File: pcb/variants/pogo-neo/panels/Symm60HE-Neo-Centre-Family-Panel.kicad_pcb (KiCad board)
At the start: 2 copper layers, 73.4 x 52.4 mm, 102 parts

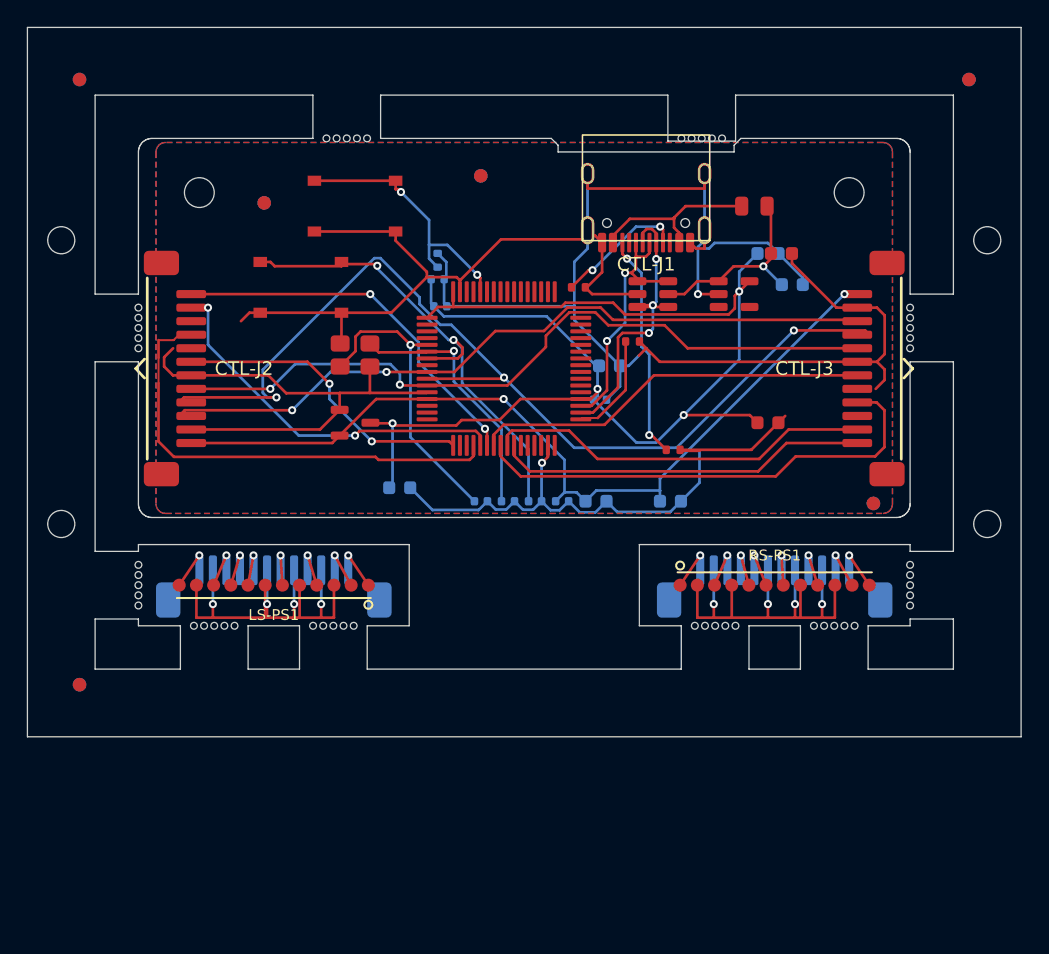
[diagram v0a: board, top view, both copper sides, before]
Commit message: Controller 57 x 27 mm straight rear edge; FPC jumpers into ZIF connectors; Neo Ergo mounting topology
Extend the former local J1 setback across the complete rear edge of the FFC
daughterboard and the Neo controller so the HRO USB-C shell projects 1.0 mm
beyond one straight wall; no component or trace moves. Regenerate all
fabrication releases, panels, Fusion references and renders for the 57 x 27 mm
outline; all twelve DRC reports are clean.

Re-specify the four board interconnects as custom 12-conductor FPC jumpers
with 0.3 mm reinforced same-side tails into the BOOMELE C20111 ZIF connectors
(length TBD from the case route) and update the BOM, READMEs and generators
accordingly. Document that the spring-head modules follow the Neo Ergo
daughterboard mounting topology.

Strip 642 macOS AppleDouble files, rebuild the four JLCPCB and pogo16 Gerber
ZIPs they had been swept into, recompute those checksum lists, and make
release.py and release_pogo16.py skip ._* and .DS_Store like the Neo
generators already do.

Co-Authored-By: Claude Opus 5 <noreply@anthropic.com>
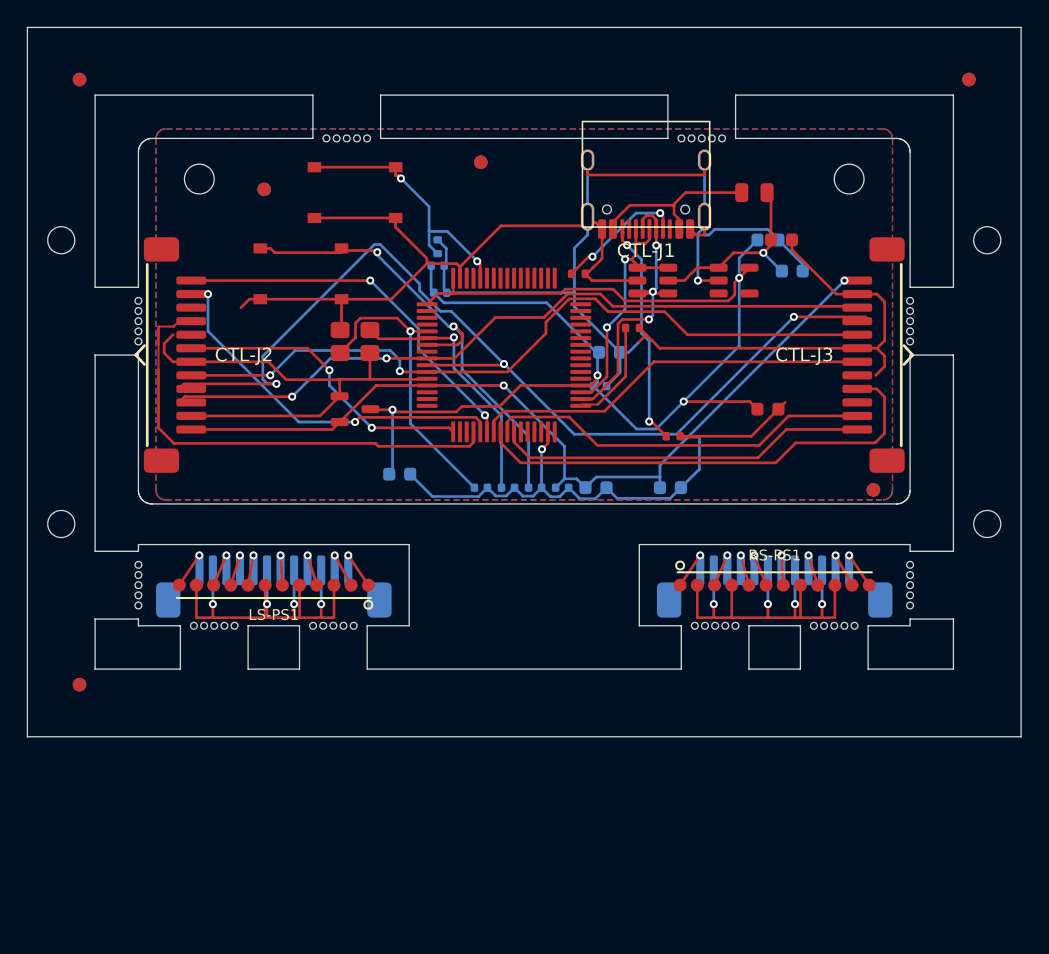
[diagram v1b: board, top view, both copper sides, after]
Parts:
- moved CTL-C1 1.00 mm to (47.5, 7.50)
- moved CTL-C10 1.00 mm to (33.8, 25.8)
- moved CTL-C11 1.00 mm to (29.3, 25.8)
- moved CTL-C12 1.00 mm to (48.3, 9.80)
- moved CTL-C13 1.00 mm to (46.5, 7.50)
- moved CTL-C14 1.00 mm to (19.3, 24.8)
- moved CTL-C15 1.00 mm to (39.3, 25.8)
- moved CTL-C2 1.00 mm to (46.5, 20.0)
- moved CTL-C3 1.00 mm to (25.3, 25.8)
- moved CTL-C4 1.00 mm to (27.3, 25.8)
- moved CTL-C5 1.00 mm to (22.3, 11.4)
- moved CTL-C6 1.00 mm to (34.1, 18.3)
- moved CTL-C7 1.00 mm to (22.1, 9.40)
- moved CTL-C8 1.00 mm to (34.8, 15.8)
- moved CTL-C9 1.00 mm to (31.3, 25.8)
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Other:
- outline, holes or cut-outs redrawn

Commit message: Replace the project with the reorganised T7 tree: ribbon keyboard is production, pogo archived
Production design is now the outward-facing FPC keyboard with per-key
SK6812MINI-E reverse-mount LEDs, a fifth SN74LV4051A mux per half so every
alternate Hall position has its own channel, an SN74AHCT1G125 LED level
shifter, a 50 x 31 mm daughterboard, 1.5 mm POM plates and 3 degree / 7 degree
tent and typing angles. The universal half panel is fully populated (359
placements) with routed NPTH alignment slots for the mutually exclusive
positions, and eight fixed-layout Left/Right PCB pairs are released under
release/layout-pcbs/ with matching BOM, CPL, Gerber ZIP, drill report and DRC.

Reorganise tools/ into cad/, generators/, layouts/, pcb/, pogo/, releases/ and
rendering/ subpackages; add designs/ and layout/ (KLE) trees and per-layout
gallery renders. The Fusion handoff is a fourteen-body reference STEP with
Gateron KS-20 switch and Cherry-profile keycap references and exact BOOMELE,
HRO and XKB models under case/fusion360/models/official/ with provenance.

The Neo-style pogo variant, its Mill-Max vendor models, the Fusion setup
script and the pogo release packages are archived as design history and
marked DO-NOT-ORDER. Their restored BOM snapshots had reintroduced the wrong
mux part C7792; corrected to C128414 / SN74LV4051ADR and their checksum lists
and archives rebuilt.

Co-Authored-By: Claude Opus 5 <noreply@anthropic.com>
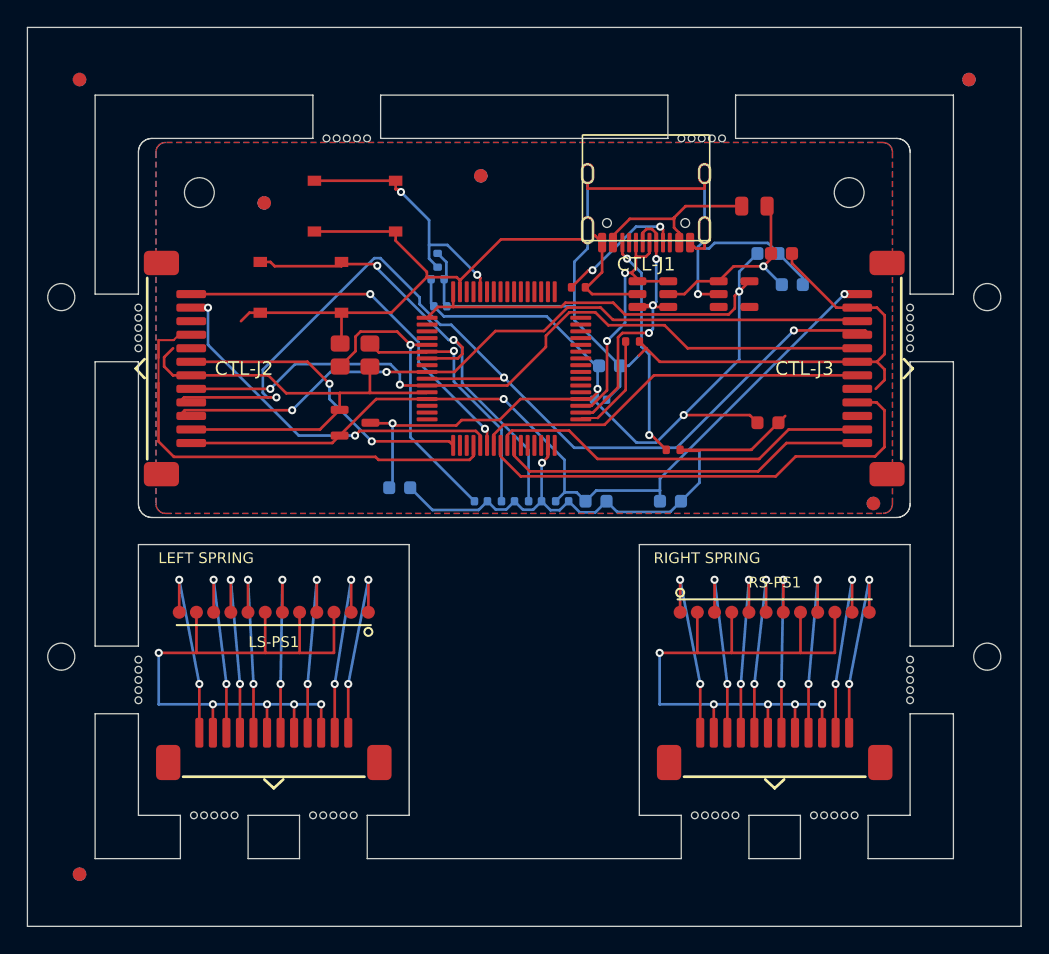
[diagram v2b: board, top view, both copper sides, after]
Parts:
- LS-JF1, RS-JF1: moved to F.Cu
- moved FIDB3 14.0 mm to (-4.35, 54.4)
- moved FIDF3 14.0 mm to (-4.35, 54.4)
- moved MB21 14.0 mm to (4.10, 50.0)
- moved MB22 14.0 mm to (4.85, 50.0)
- moved MB23 14.0 mm to (5.60, 50.0)
- moved MB24 14.0 mm to (6.35, 50.0)
- moved MB25 14.0 mm to (7.10, 50.0)
- moved MB26 14.0 mm to (12.9, 50.0)
- moved MB27 14.0 mm to (13.7, 50.0)
- moved MB28 14.0 mm to (14.4, 50.0)
- moved MB29 14.0 mm to (15.2, 50.0)
- moved MB30 14.0 mm to (15.9, 50.0)
- moved MB36 14.0 mm to (41.1, 50.0)
- moved MB37 14.0 mm to (41.9, 50.0)
- moved MB38 14.0 mm to (42.6, 50.0)
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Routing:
- net /LS/GND: track 33.8 -> 49.1 mm, vias 4 -> 5
- net /RS/GND: track 33.8 -> 49.1 mm, vias 4 -> 5
- net /RS/ADC_R1: track 3.30 -> 13.7 mm, vias 1 -> 2
- net /LS/ADC_L1: track 3.30 -> 13.7 mm, vias 1 -> 2
- net /LS/MUX_A2: track 3.34 -> 13.7 mm, vias 1 -> 2
- net /RS/MUX_A1: track 3.38 -> 13.7 mm, vias 1 -> 2
- net /RS/ADC_R2: track 3.40 -> 13.7 mm, vias 1 -> 2
- net /LS/MUX_A1: track 3.40 -> 13.7 mm, vias 1 -> 2
- net /LS/ADC_L2: track 3.40 -> 13.7 mm, vias 1 -> 2
- net /RS/MUX_A2: track 3.46 -> 13.7 mm, vias 1 -> 2
- net /RS/MUX_A0: track 3.49 -> 13.8 mm, vias 1 -> 2
- net /LS/MUX_A0: track 3.49 -> 13.8 mm, vias 1 -> 2
- net /RS/ADC_R3: track 3.61 -> 13.8 mm, vias 1 -> 2
- net /LS/ADC_L3: track 3.61 -> 13.8 mm, vias 1 -> 2
- net /LS/+3V3A: track 3.75 -> 13.8 mm, vias 1 -> 2
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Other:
- board size 73.4 x 52.4 mm -> 73.4 x 66.4 mm
- board text added: "LEFT SPRING"
- board text added: "RIGHT SPRING"

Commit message: Neo-pogo: 3 deg tent, 7 deg typing, 20 x 6 mm spring heads; integrated Fusion reference
Regenerate the five Neo boards, both family panels, and the JLCPCB and
PCBWay release packages for the narrower floating spring heads and the
controller mounted left-to-right under the centre blocker. Rebuild the Fusion
reference set around a single integrated master STEP
(Symm60HE-case-reference-assembly.step) and rewrite the Fusion setup script
to import it as one grounded assembly.

Strip macOS AppleDouble (._*) files that a Mac copy introduced: they had been
swept into every PCBWay Gerber ZIP, both release archives and the SHA256SUMS
lists. Rebuild those archives and checksums, make both release generators skip
._* and .DS_Store, and ignore ._* and .recovery/ in git.

Co-Authored-By: Claude Opus 5 <noreply@anthropic.com>
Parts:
- LS-JF1, RS-JF1: moved to B.Cu
- moved FIDB3 14.0 mm to (-4.35, 40.4)
- moved FIDF3 14.0 mm to (-4.35, 40.4)
- moved MB21 14.0 mm to (4.10, 36.0)
- moved MB22 14.0 mm to (4.85, 36.0)
- moved MB23 14.0 mm to (5.60, 36.0)
- moved MB24 14.0 mm to (6.35, 36.0)
- moved MB25 14.0 mm to (7.10, 36.0)
- moved MB26 14.0 mm to (12.9, 36.0)
- moved MB27 14.0 mm to (13.7, 36.0)
- moved MB28 14.0 mm to (14.4, 36.0)
- moved MB29 14.0 mm to (15.2, 36.0)
- moved MB30 14.0 mm to (15.9, 36.0)
- moved MB36 14.0 mm to (41.1, 36.0)
- moved MB37 14.0 mm to (41.9, 36.0)
- moved MB38 14.0 mm to (42.6, 36.0)
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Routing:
- net /RS/GND: track 49.1 -> 33.8 mm, vias 5 -> 4
- net /LS/GND: track 49.1 -> 33.8 mm, vias 5 -> 4
- net /RS/ADC_R1: track 13.7 -> 3.30 mm, vias 2 -> 1
- net /LS/ADC_L1: track 13.7 -> 3.30 mm, vias 2 -> 1
- net /LS/MUX_A2: track 13.7 -> 3.34 mm, vias 2 -> 1
- net /RS/MUX_A1: track 13.7 -> 3.38 mm, vias 2 -> 1
- net /RS/ADC_R2: track 13.7 -> 3.40 mm, vias 2 -> 1
- net /LS/MUX_A1: track 13.7 -> 3.40 mm, vias 2 -> 1
- net /LS/ADC_L2: track 13.7 -> 3.40 mm, vias 2 -> 1
- net /RS/MUX_A2: track 13.7 -> 3.46 mm, vias 2 -> 1
- net /RS/MUX_A0: track 13.8 -> 3.49 mm, vias 2 -> 1
- net /LS/MUX_A0: track 13.8 -> 3.49 mm, vias 2 -> 1
- net /RS/ADC_R3: track 13.8 -> 3.61 mm, vias 2 -> 1
- net /LS/ADC_L3: track 13.8 -> 3.61 mm, vias 2 -> 1
- net /LS/+3V3A: track 13.8 -> 3.75 mm, vias 2 -> 1
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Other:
- board size 73.4 x 66.4 mm -> 73.4 x 52.4 mm
- board text removed: "LEFT SPRING"
- board text removed: "RIGHT SPRING"
